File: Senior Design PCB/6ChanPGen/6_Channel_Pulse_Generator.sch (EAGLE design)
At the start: 84 parts, among them U1 AD8619ARZ, U2 AD8619ARZ, U3 AD8619ARZ

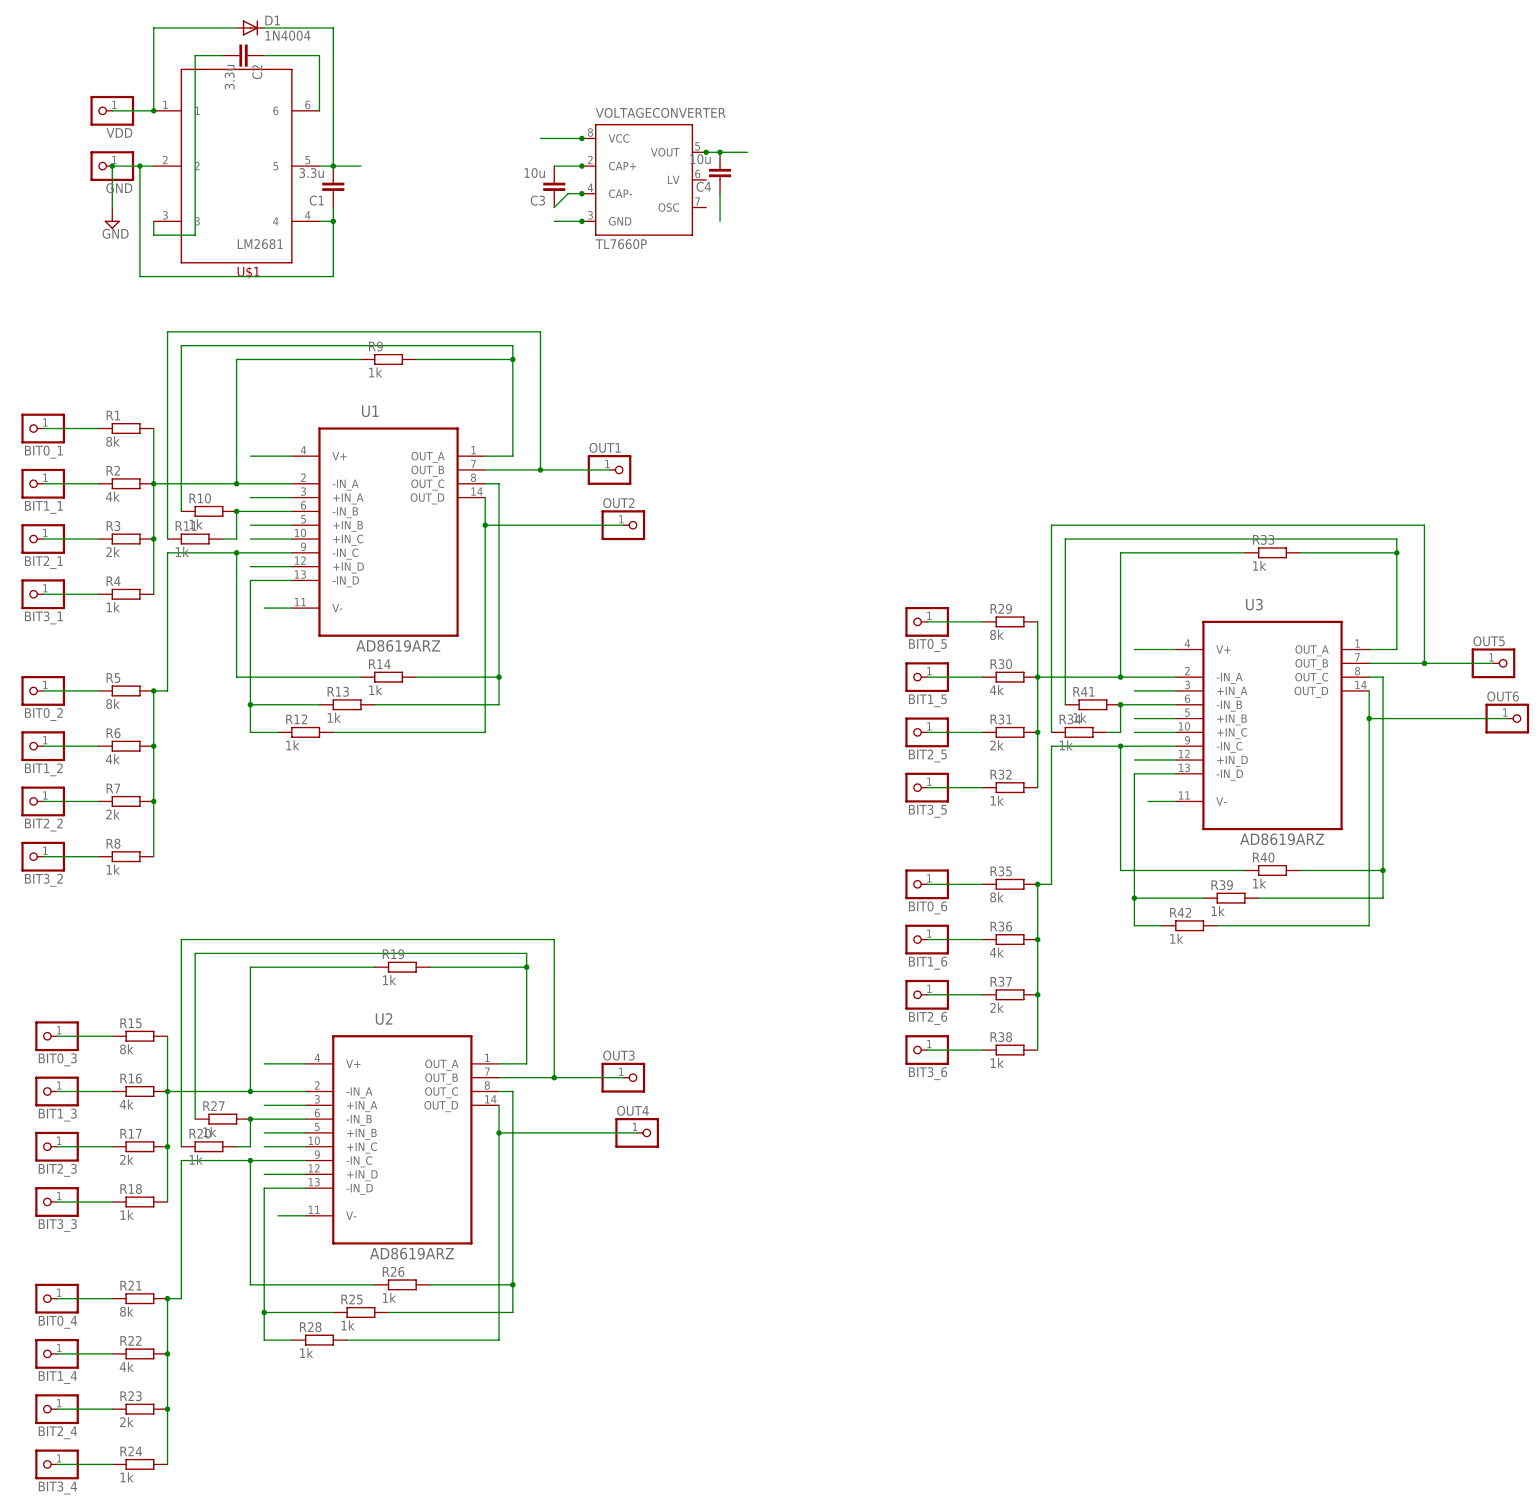
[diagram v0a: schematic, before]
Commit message: Added BOMs, versions for assembly instructions
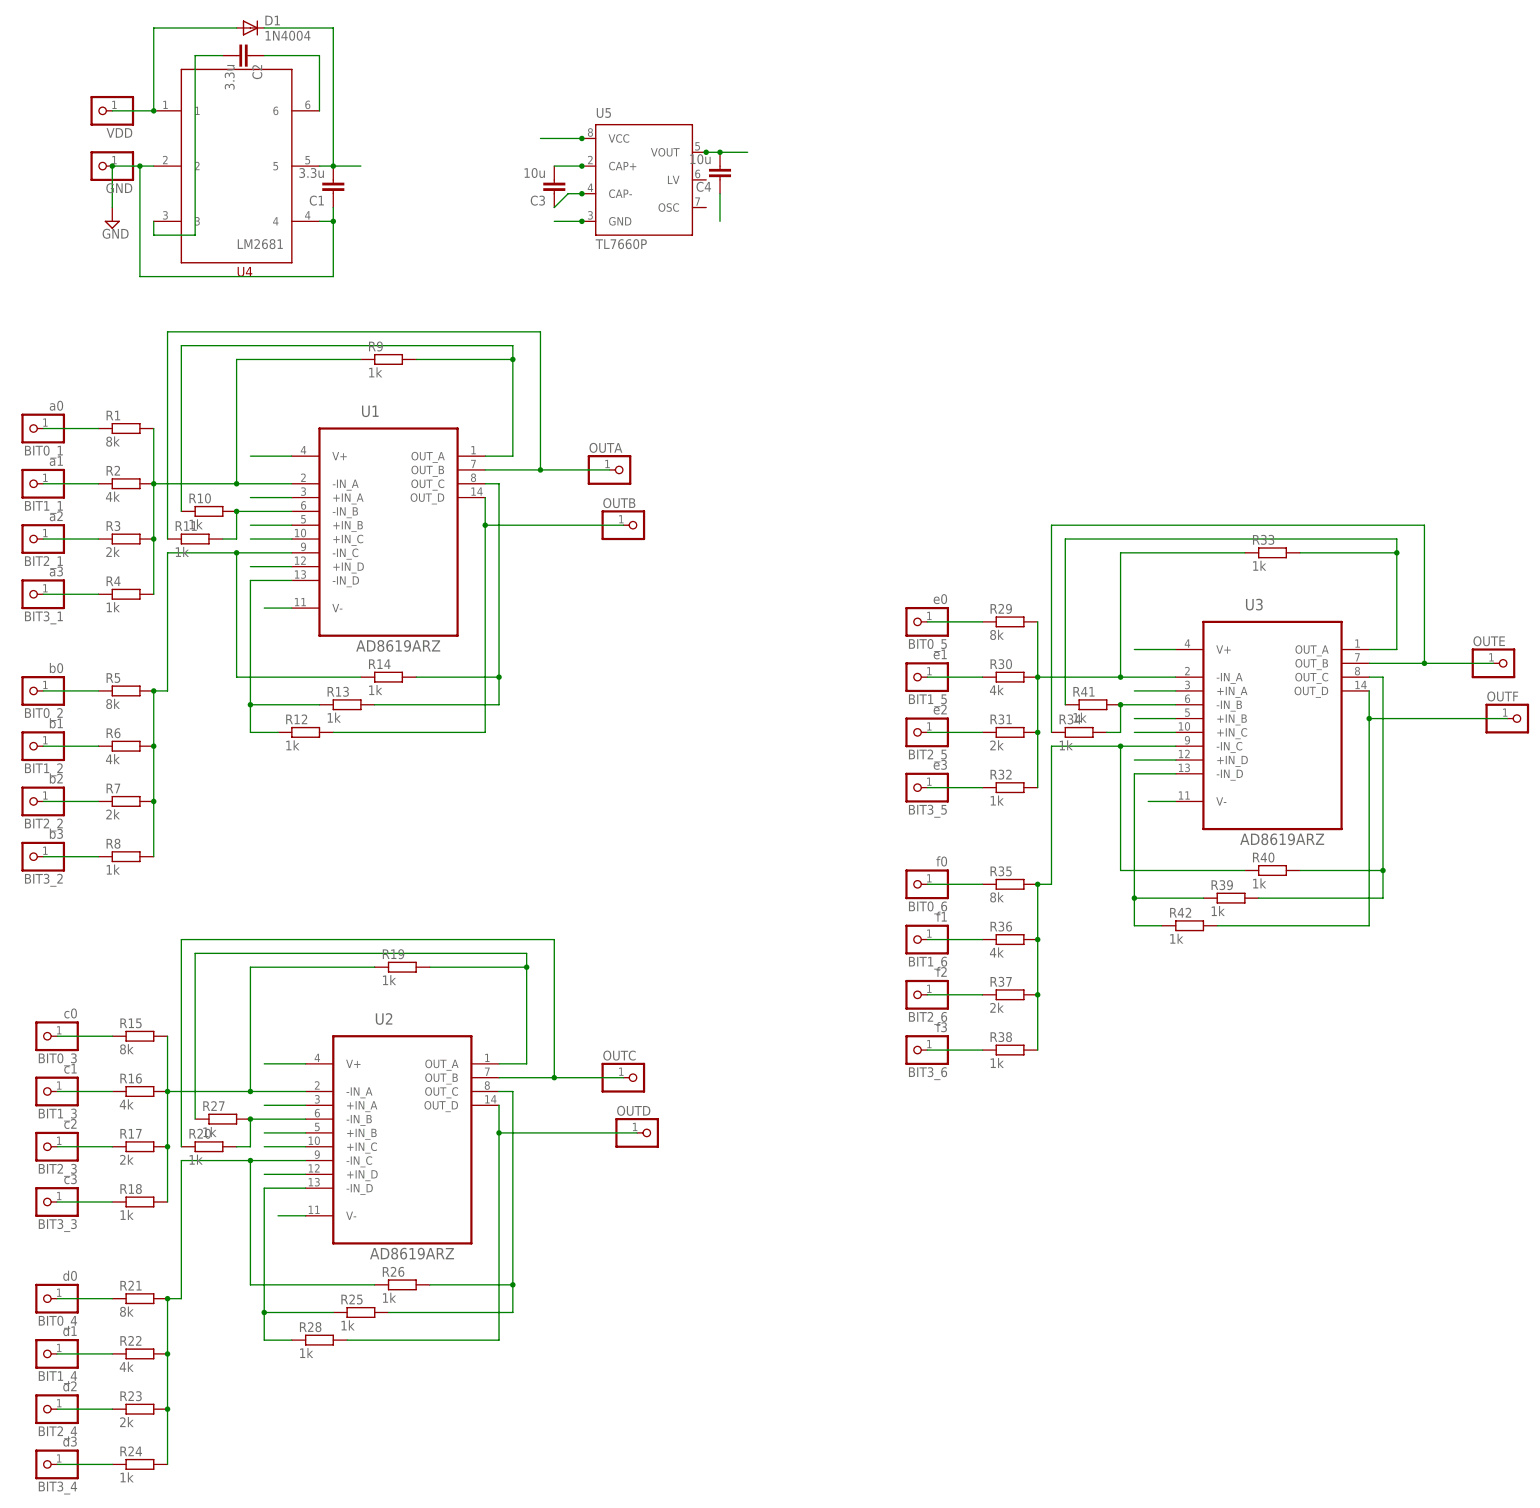
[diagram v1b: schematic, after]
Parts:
- BIT0_1: value (none) -> a0
- BIT0_2: value (none) -> b0
- BIT0_3: value (none) -> c0
- BIT0_4: value (none) -> d0
- BIT0_5: value (none) -> e0
- BIT0_6: value (none) -> f0
- BIT1_1: value (none) -> a1
- BIT1_2: value (none) -> b1
- BIT1_3: value (none) -> c1
- BIT1_4: value (none) -> d1
- BIT1_5: value (none) -> e1
- BIT1_6: value (none) -> f1
- BIT2_1: value (none) -> a2
- BIT2_2: value (none) -> b2
- BIT2_3: value (none) -> c2
- BIT2_4: value (none) -> d2
- BIT2_5: value (none) -> e2
- BIT2_6: value (none) -> f2
- BIT3_1: value (none) -> a3
- BIT3_2: value (none) -> b3
- BIT3_3: value (none) -> c3
- BIT3_4: value (none) -> d3
- BIT3_5: value (none) -> e3
- BIT3_6: value (none) -> f3
- renumbered OUT1 to OUTA, OUT2 to OUTB, OUT3 to OUTC, OUT4 to OUTD, OUT5 to OUTE, OUT6 to OUTF, U$1 to U4, VOLTAGECONVERTER to U5
